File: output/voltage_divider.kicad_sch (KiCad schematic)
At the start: 3 parts

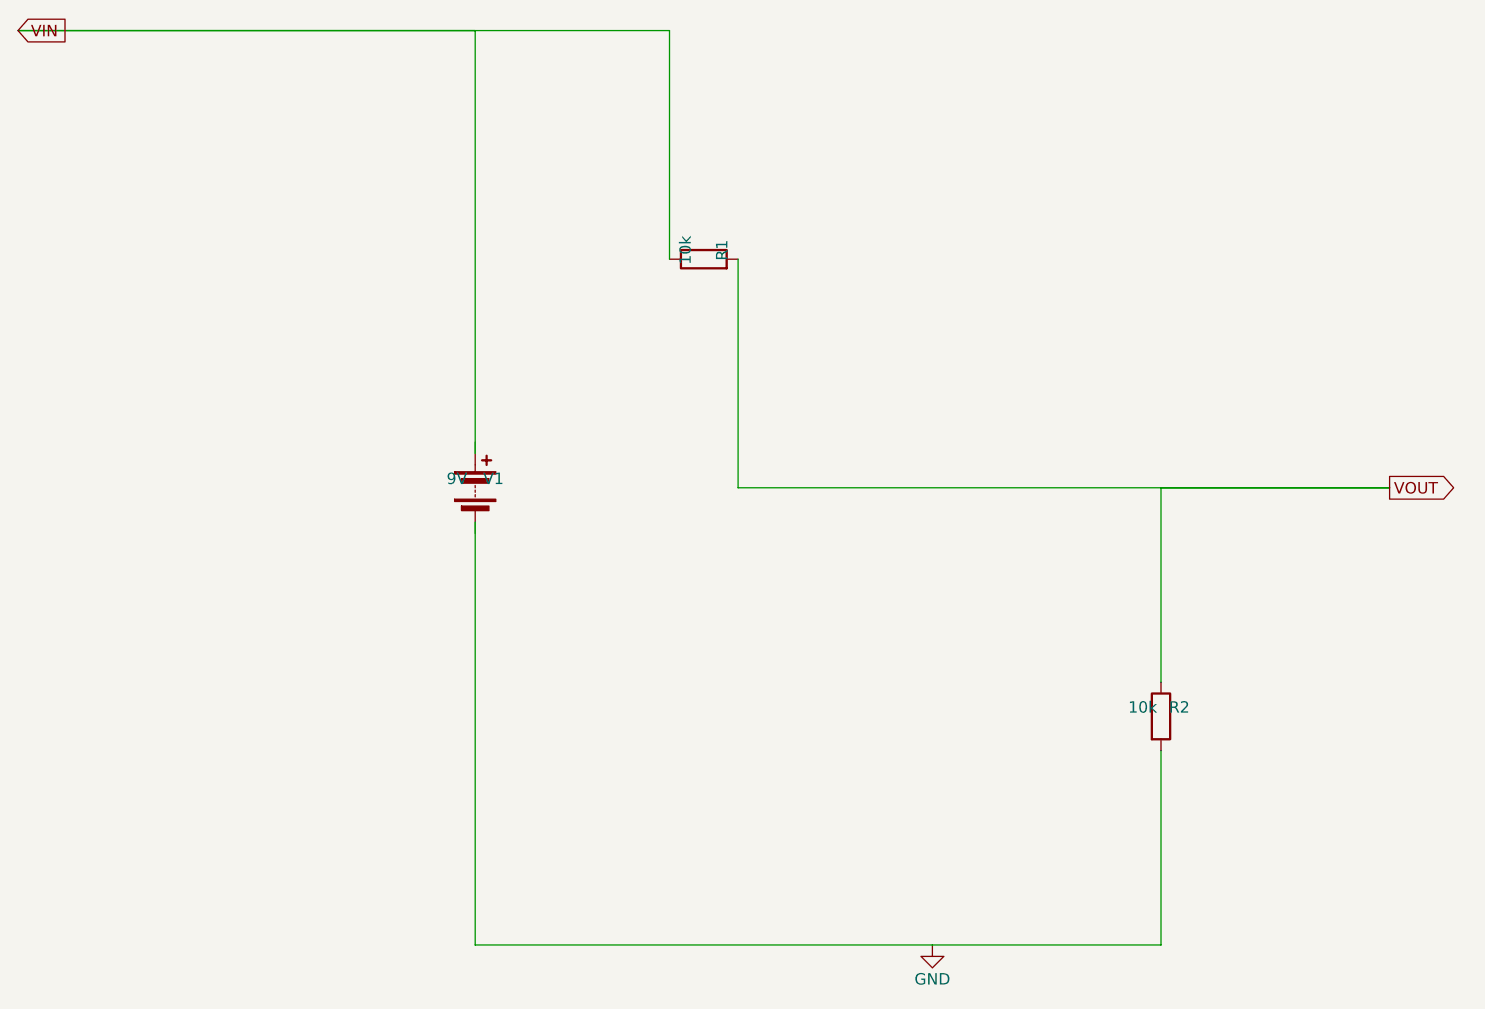
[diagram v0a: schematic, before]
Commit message: refactor: change placement engine, kicad_gen.py, add spring based layout
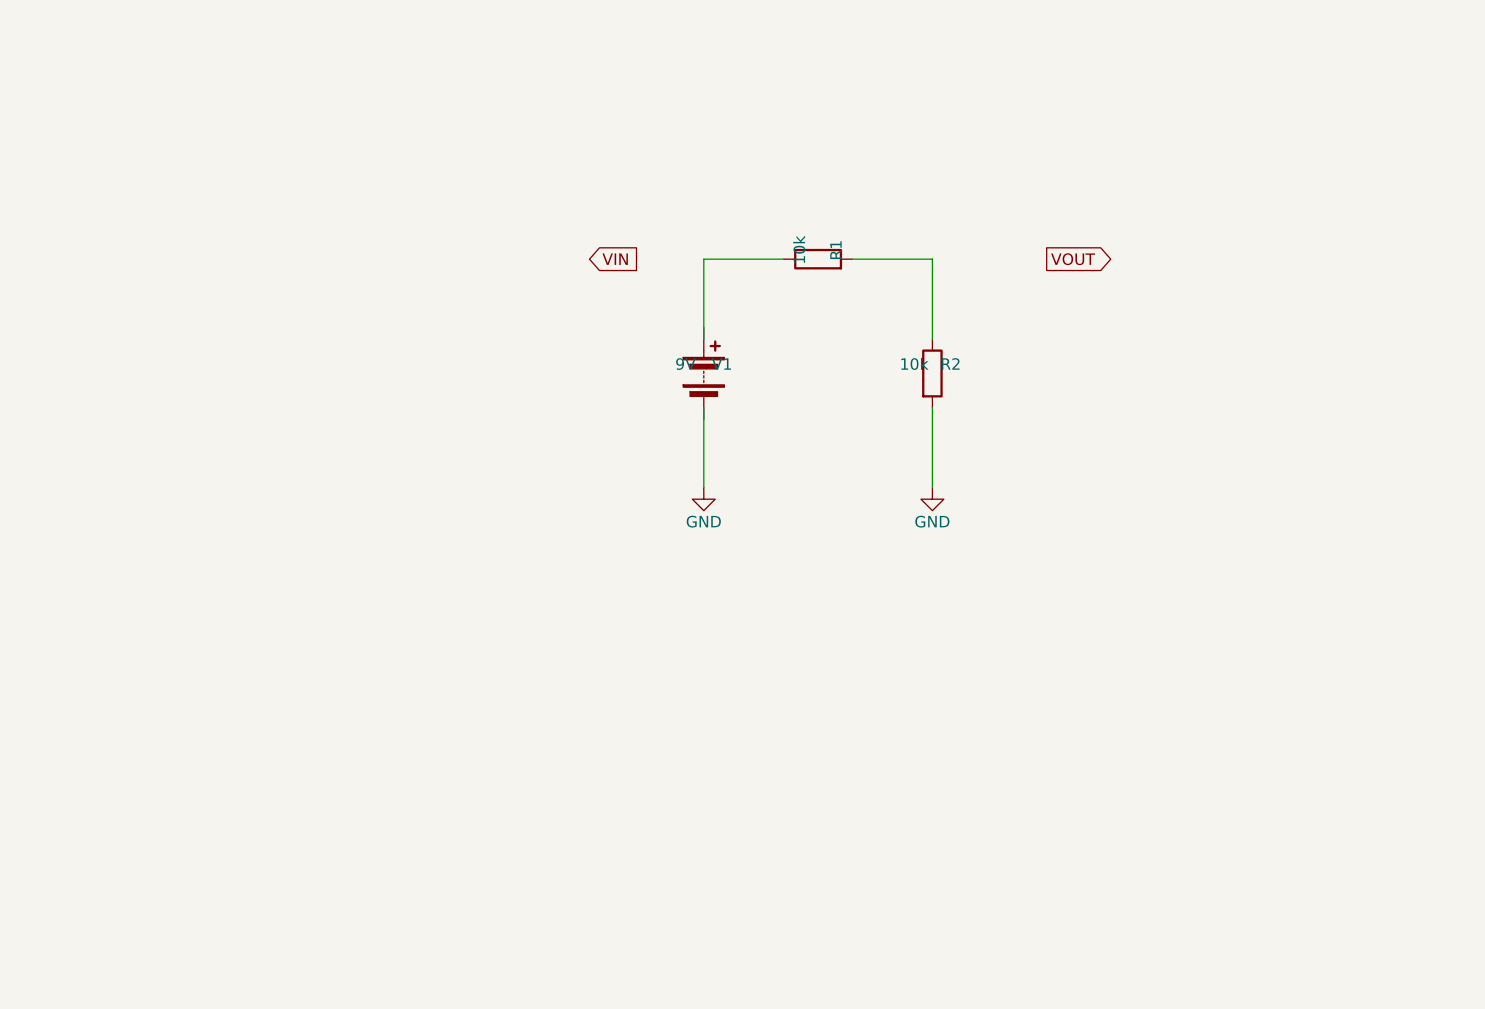
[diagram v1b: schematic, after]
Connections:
- net VIN: no longer R1.1
- net VOUT: no longer R1.2, R2.1
- new net: R1.2, R2.1
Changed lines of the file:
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@@
   (symbol
     (lib_id "Device:Battery")
-    (at 124.6 125.4 0)
+    (at 150.0 112.7 0)
     (unit 1)
     (in_bom yes)
     (on_board yes)
     (property "Reference" "V1"
-      (at 126.632 124.4 0)
+      (at 152.032 111.7 0)
       (effects (font (size 1.27 1.27)))
     )
     (property "Value" "9V"
-      (at 122.568 124.4 0)
+      (at 147.968 111.7 0)
       (effects (font (size 1.27 1.27)))
     )
@@
     (instances
       (project "schematic"
-        (path "/992e6e80-9f74-4d6b-9677-e9da05d86bcc"
+        (path "/8d6ab1ba-8a61-4ffd-b9c6-a5cd288c6016"
           (reference "V1")
           (unit 1)
@@
   (symbol
     (lib_id "Device:R")
-    (at 150.0 100.0 90)
+    (at 162.7 100.0 90)
     (unit 1)
     (in_bom yes)
     (on_board yes)
     (property "Reference" "R1"
-      (at 152.032 99.0 0)
+      (at 164.732 99.0 0)
       (effects (font (size 1.27 1.27)))
     )
     (property "Value" "10k"
-      (at 147.968 99.0 0)
+      (at 160.668 99.0 0)
       (effects (font (size 1.27 1.27)))
     )
@@
     (instances
       (project "schematic"
-        (path "/992e6e80-9f74-4d6b-9677-e9da05d86bcc"
+        (path "/8d6ab1ba-8a61-4ffd-b9c6-a5cd288c6016"
           (reference "R1")
           (unit 1)
@@
   (symbol
     (lib_id "Device:R")
-    (at 200.8 150.8 0)
+    (at 175.4 112.7 0)
     (unit 1)
     (in_bom yes)
     (on_board yes)
     (property "Reference" "R2"
-      (at 202.832 149.8 0)
+      (at 177.432 111.7 0)
       (effects (font (size 1.27 1.27)))
     )
     (property "Value" "10k"
-      (at 198.768 149.8 0)
+      (at 173.368 111.7 0)
       (effects (font (size 1.27 1.27)))
     )
@@
     (instances
       (project "schematic"
-        (path "/992e6e80-9f74-4d6b-9677-e9da05d86bcc"
+        (path "/8d6ab1ba-8a61-4ffd-b9c6-a5cd288c6016"
           (reference "R2")
           (unit 1)
@@
   (symbol
     (lib_id "power:GND")
-    (at 175.4 176.2 0)
+    (at 150.0 125.4 0)
     (unit 1)
     (in_bom yes)
     (on_board yes)
     (property "Reference" "#PWR01"
-      (at 175.4 182.55 0)
+      (at 150.0 131.75 0)
       (effects (font (size 1.27 1.27)) hide)
     )
     (property "Value" "GND"
-      (at 175.4 180.01 0)
+      (at 150.0 129.21 0)
       (effects (font (size 1.27 1.27)))
     )
@@
     (instances
       (project "schematic"
-        (path "/992e6e80-9f74-4d6b-9677-e9da05d86bcc"
+        (path "/8d6ab1ba-8a61-4ffd-b9c6-a5cd288c6016"
           (reference "#PWR01")
+          (unit 1)
+        )
+      )
+    )
+  )
+  (symbol
+    (lib_id "power:GND")
+    (at 175.4 125.4 0)
+    (unit 1)
+    (in_bom yes)
+    (on_board yes)
+    (property "Reference" "#PWR02"
+      (at 175.4 131.75 0)
+      (effects (font (size 1.27 1.27)) hide)
+    )
+    (property "Value" "GND"
+      (at 175.4 129.21 0)
+      (effects (font (size 1.27 1.27)))
+    )
+    (property "Footprint" "" (at 0 0 0)
+      (effects (font (size 1.27 1.27)) hide)
+    )
+    (property "Datasheet" "" (at 0 0 0)
+      (effects (font (size 1.27 1.27)) hide)
+    )
+    (instances
+      (project "schematic"
+        (path "/8d6ab1ba-8a61-4ffd-b9c6-a5cd288c6016"
+          (reference "#PWR02")
           (unit 1)
         )
@@
   (global_label "VIN"
     (shape input)
-    (at 73.8 74.6 0)
+    (at 137.3 100.0 0)
     (fields_autoplaced yes)
     (effects (font (size 1.27 1.27)))
@@
   (global_label "VOUT"
     (shape output)
-    (at 226.2 125.4 0)
+    (at 188.1 100.0 0)
     (fields_autoplaced yes)
     (effects (font (size 1.27 1.27)))
@@
   )
   (wire
-    (pts (xy 73.8 74.6) (xy 124.6 74.6))
+    (pts (xy 150.0 100.0) (xy 150.0 108.89))
     (stroke (width 0) (type default))
   )
   (wire
-    (pts (xy 124.6 74.6) (xy 124.6 121.59))
+    (pts (xy 150.0 125.4) (xy 150.0 116.51))
     (stroke (width 0) (type default))
   )
   (wire
-    (pts (xy 175.4 176.2) (xy 124.6 176.2))
+    (pts (xy 150.0 100.0) (xy 158.89 100.0))
     (stroke (width 0) (type default))
   )
   (wire
-    (pts (xy 124.6 176.2) (xy 124.6 129.21))
+    (pts (xy 175.4 100.0) (xy 166.51 100.0))
     (stroke (width 0) (type default))
   )
   (wire
-    (pts (xy 73.8 74.6) (xy 146.19 74.6))
+    (pts (xy 175.4 100.0) (xy 175.4 108.89))
     (stroke (width 0) (type default))
   )
   (wire
-    (pts (xy 146.19 74.6) (xy 146.19 100.0))
+    (pts (xy 175.4 125.4) (xy 175.4 116.51))
     (stroke (width 0) (type default))
   )
-  (wire
-    (pts (xy 226.2 125.4) (xy 153.81 125.4))
-    (stroke (width 0) (type default))
-  )
-  (wire
-    (pts (xy 153.81 125.4) (xy 153.81 100.0))
-    (stroke (width 0) (type default))
-  )
-  (wire
-    (pts (xy 226.2 125.4) (xy 200.8 125.4))
-    (stroke (width 0) (type default))
-  )
-  (wire
-    (pts (xy 200.8 125.4) (xy 200.8 146.99))
-    (stroke (width 0) (type default))
-  )
-  (wire
-    (pts (xy 175.4 176.2) (xy 200.8 176.2))
-    (stroke (width 0) (type default))
-  )
-  (wire
-    (pts (xy 200.8 176.2) (xy 200.8 154.61))
-    (stroke (width 0) (type default))
-  )

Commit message: feat: revise pipeline
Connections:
- net VIN: now also R1.1
- net VOUT: now also R1.2, R2.1
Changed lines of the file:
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@@
     (instances
       (project "schematic"
-        (path "/8d6ab1ba-8a61-4ffd-b9c6-a5cd288c6016"
+        (path "/dbbcfe0e-2bfa-4b7d-88b2-361c2dcb19ad"
           (reference "V1")
           (unit 1)
@@
     (instances
       (project "schematic"
-        (path "/8d6ab1ba-8a61-4ffd-b9c6-a5cd288c6016"
+        (path "/dbbcfe0e-2bfa-4b7d-88b2-361c2dcb19ad"
           (reference "R1")
           (unit 1)
@@
     (instances
       (project "schematic"
-        (path "/8d6ab1ba-8a61-4ffd-b9c6-a5cd288c6016"
+        (path "/dbbcfe0e-2bfa-4b7d-88b2-361c2dcb19ad"
           (reference "R2")
           (unit 1)
@@
     (instances
       (project "schematic"
-        (path "/8d6ab1ba-8a61-4ffd-b9c6-a5cd288c6016"
+        (path "/dbbcfe0e-2bfa-4b7d-88b2-361c2dcb19ad"
           (reference "#PWR01")
           (unit 1)
@@
     (instances
       (project "schematic"
-        (path "/8d6ab1ba-8a61-4ffd-b9c6-a5cd288c6016"
+        (path "/dbbcfe0e-2bfa-4b7d-88b2-361c2dcb19ad"
           (reference "#PWR02")
           (unit 1)
@@
   (global_label "VIN"
     (shape input)
-    (at 137.3 100.0 0)
+    (at 140.0 100.0 0)
     (fields_autoplaced yes)
     (effects (font (size 1.27 1.27)))
@@
   (global_label "VOUT"
     (shape output)
-    (at 188.1 100.0 0)
+    (at 185.4 100.0 180)
     (fields_autoplaced yes)
     (effects (font (size 1.27 1.27)))
@@
     (stroke (width 0) (type default))
   )
+  (wire
+    (pts (xy 140.0 100.0) (xy 150.0 100.0))
+    (stroke (width 0) (type default))
+  )
+  (wire
+    (pts (xy 175.4 100.0) (xy 185.4 100.0))
+    (stroke (width 0) (type default))
+  )
